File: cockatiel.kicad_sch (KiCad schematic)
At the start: 33 parts, among them J1 Programmer, J11 MIC_P_SEL, J12 MIC_N_SEL, J13 Cox Box Mic In, J14 Cox Box Mic Out, J15 Mic Out, J16 Headset/Mic In, J3 DEBUG_UART, J4 RESET, J5 Magnetic connector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

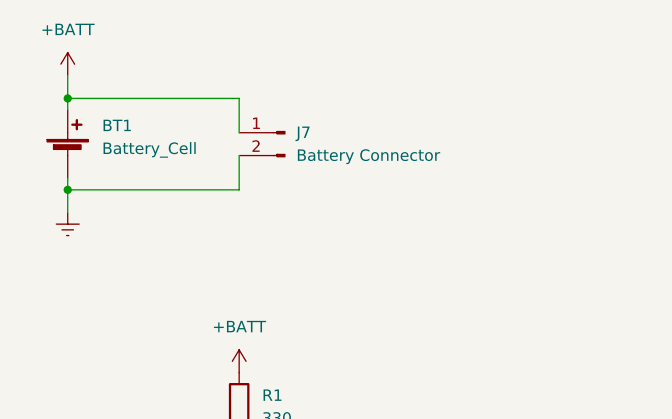
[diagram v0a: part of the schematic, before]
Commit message: Swap the battery connector pins
It seems that the de-facto setup is with pin 1 as ground, so fix it
here.
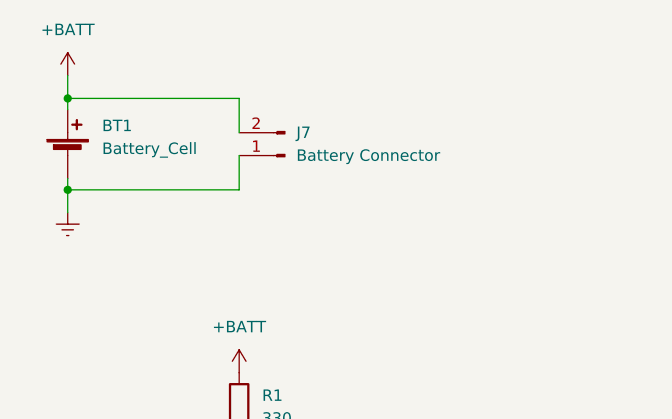
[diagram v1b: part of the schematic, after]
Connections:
- net +BATT: now also J7.2 (Pin_2); no longer J7.1 (Pin_1)
- net Earth: now also J7.1 (Pin_1); no longer J7.2 (Pin_2)
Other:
- moved on the sheet: J7
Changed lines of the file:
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@@
     (pin "2")
   )
-  (symbol (lib_id "Connector:Conn_01x02_Male") (at 43.18 27.94 0) (mirror y) (unit 1)
+  (symbol (lib_id "Connector:Conn_01x02_Male") (at 43.18 30.48 180) (unit 1)
     (in_bom yes) (on_board yes) (fields_autoplaced)
     (property "Reference" "J7" (id 0) (at 44.45 27.9399 0)
@@
       (effects (font (size 1.27 1.27)) (justify right))
     )
-    (property "Footprint" "Connector_JST:JST_PH_S2B-PH-K_1x02_P2.00mm_Horizontal" (id 2) (at 43.18 27.94 0)
+    (property "Footprint" "Connector_JST:JST_PH_S2B-PH-K_1x02_P2.00mm_Horizontal" (id 2) (at 43.18 30.48 0)
       (effects (font (size 1.27 1.27)) hide)
     )
-    (property "Datasheet" "~" (id 3) (at 43.18 27.94 0)
+    (property "Datasheet" "~" (id 3) (at 43.18 30.48 0)
       (effects (font (size 1.27 1.27)) hide)
     )
-    (property "LCSC" "C173752" (id 4) (at 44.45 27.9399 0)
+    (property "LCSC" "C173752" (id 4) (at 44.45 30.4801 0)
       (effects (font (size 1.27 1.27)) hide)
     )
